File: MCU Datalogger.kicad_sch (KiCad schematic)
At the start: 0 parts

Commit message: configure schematic
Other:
- title: (none) -> ${project_name}
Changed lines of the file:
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@@
 	(generator_version "8.0")
 	(paper "A4")
+	(title_block
+		(title "${project_name}")
+		(date "2024-09-19")
+		(rev "1")
+	)
 	(sheet_instances
 		(path "/"

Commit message: arrange schematic symbols
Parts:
- added BT1: Battery, symbol Device:Battery
- added C1, C2, C3, C4: C, symbol Device:C
- added C5: C_Polarized, symbol Device:C_Polarized
- added D1, D2: LED, symbol Device:LED
- added H1, H2, H3, H4: MountingHole, symbol Mechanical:MountingHole
- added R1, R2, R3, R4, R5, R6, R7: R, symbol Device:R
- added U1, U2: 24LC1025, symbol Memory_EEPROM:24LC1025
- added U3: DS1337S_T_R, DS1337S_T_R:SOIC127P600X175-8N, symbol DS1337S_T_R:DS1337S_T_R
- added U4: ATMEGA328P-AN, ATMEGA328P-AN:QFP80P900X900X120-32N, symbol ATMEGA328P-AN:ATMEGA328P-AN
- added Y1, Y2: Crystal, symbol Device:Crystal
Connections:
- new net: U4.21 (GND), U4.3 (GND), U4.5 (GND)
- new net: U4.4 (VCC), U4.6 (VCC)
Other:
- added sheet Connectors (conenctors.kicad_sch)

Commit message: assign footprints
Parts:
- BT1: footprint (none) -> Connector_PinHeader_2.54mm:PinHeader_1x02_P2.54mm_Vertical
- C1, C2: value C -> 22pF; footprint (none) -> Capacitor_SMD:C_0805_2012Metric
- C3, C4: value C -> 0.1uF; footprint (none) -> Capacitor_SMD:C_0805_2012Metric
- C5: value C_Polarized -> 100nF; footprint (none) -> Capacitor_SMD:C_0805_2012Metric
- D1, D2: footprint (none) -> LED_SMD:LED_0805_2012Metric
- H1, H2, H3, H4: footprint (none) -> MountingHole:MountingHole_2.1mm
- R1, R2: value R -> 4.7K; footprint (none) -> Resistor_SMD:R_0805_2012Metric
- R3, R5: value R -> 330; footprint (none) -> Resistor_SMD:R_0805_2012Metric
- R4, R6, R7: value R -> 10K; footprint (none) -> Resistor_SMD:R_0805_2012Metric
- U1, U2: footprint (none) -> Package_SO:SOIC-8_5.23x5.23mm_P1.27mm
- Y1: value Crystal -> 32.768 KHz; footprint (none) -> Crystal:Crystal_SMD_5032-2Pin_5.0x3.2mm_HandSoldering
- Y2: value Crystal -> 16 MHz; footprint (none) -> Crystal:Crystal_SMD_5032-2Pin_5.0x3.2mm_HandSoldering
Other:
- moved on the sheet: C3, C5, R7, Y1

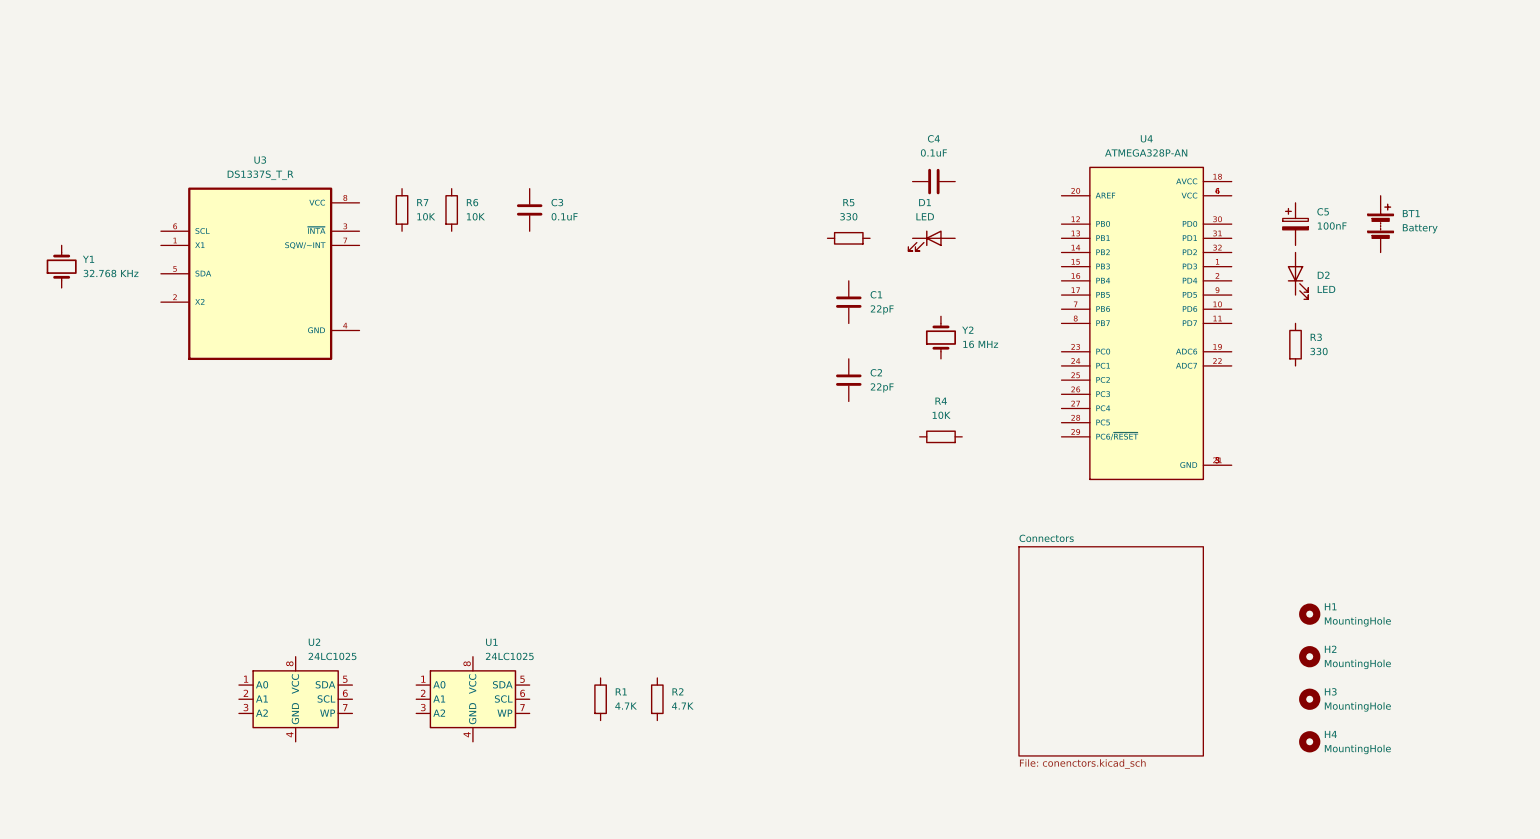
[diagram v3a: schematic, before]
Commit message: wire main scheme sheet
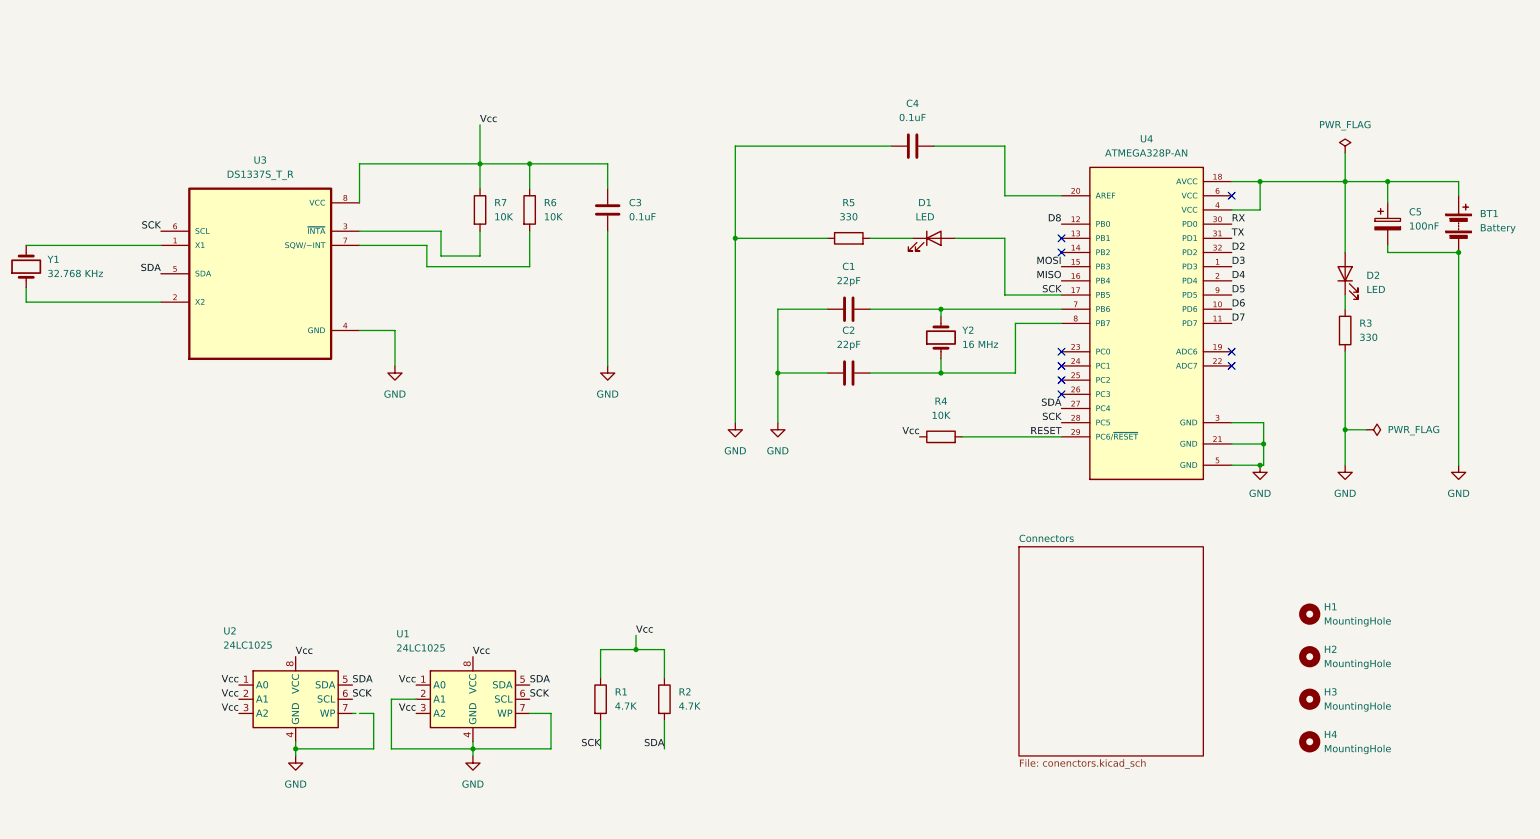
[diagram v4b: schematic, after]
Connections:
- net at Y1.1: now also U3.2 (X2)
- net at Y1.2: now also U3.1 (X1)
- net GND: now reaches C1.1
- net GND: now also BT1.2 (-), C2.1, C3.2, C4.1, C5.2, R3.2, R5.1, U1.2 (A1), U1.4 (GND), U1.7 (WP), U2.4 (GND), U3.4 (GND), U4.21 (GND), U4.3 (GND), U4.5 (GND)
- net at C1.2: now also U4.7 (PB6), Y2.2
- net Vcc: now reaches R4.1
- net Vcc: now also C3.1, R1.1, R2.1, R6.1, R7.1, U1.1 (A0), U1.3 (A2), U1.8 (VCC), U2.1 (A0), U2.2 (A1), U2.3 (A2), U2.8 (VCC), U3.8 (VCC)
- net RESET: now reaches R4.2
- net RESET: now also U4.29 (PC6/~{RESET})
- net at R6.2: now also U3.7 (SQW/~INT)
- net at R3.1: now also D2.1 (K)
- net at U3.3 (~{INTA}): now also R7.2
- net SDA: now reaches U3.5 (SDA)
- net SDA: now also R2.2, U1.5 (SDA), U2.5 (SDA), U4.27 (PC4)
- net SCK: now reaches U3.6 (SCL)
- net SCK: now also D1.2 (A), R1.2, U1.6 (SCL), U2.6 (SCL), U4.17 (PB5), U4.28 (PC5)
- net at BT1.1 (+): now also C5.1, D2.2 (A), U4.18 (AVCC), U4.4 (VCC)
- net at Y2.1: now also C2.2, U4.8 (PB7)
- net at D1.1 (K): now also R5.2
- net at C4.2: now also U4.20 (AREF)
- net D3: now reaches U4.1 (PD3)
- net D6: now reaches U4.10 (PD6)
- net D7: now reaches U4.11 (PD7)
- net D8: now reaches U4.12 (PB0)
- net MOSI: now reaches U4.15 (PB3)
- net MISO: now reaches U4.16 (PB4)
- net D4: now reaches U4.2 (PD4)
- net RX: now reaches U4.30 (PD0)
- net TX: now reaches U4.31 (PD1)
- net D2: now reaches U4.32 (PD2)
- net at U4.6 (VCC): no longer U4.4 (VCC)
- net D5: now reaches U4.9 (PD5)
- no-connect marks 0 -> 9
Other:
- moved on the sheet: BT1, C1, C2, C3, C4, C5, D2, R2, R3, R6, R7, Y1

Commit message: complete wiring and perform ERC
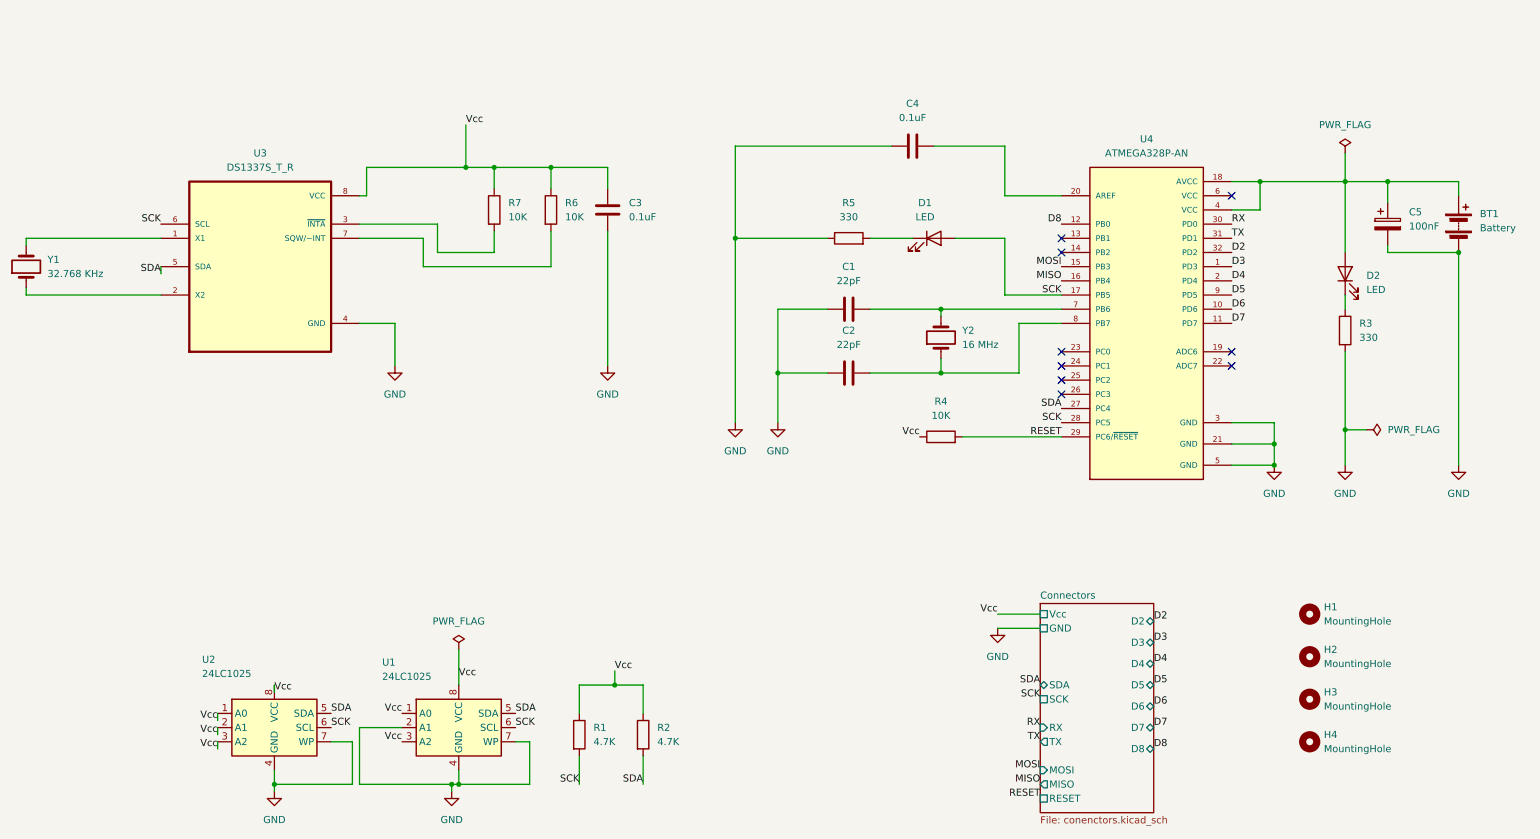
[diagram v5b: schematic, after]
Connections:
- net GND: now also U2.7 (WP)
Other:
- sheet Connectors ports: added D2, D3, D4, D5, D6, D7, D8, GND, MISO, MOSI, RESET, RX, SCK, SDA, TX, Vcc; removed none
- moved on the sheet: R1, R2, R6, R7, U1, U2, U3

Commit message: fix bugs
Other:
- note added: "EEPROM"
- note added: "MCU"
- note added: "Mounting"
- note added: "Real Time Clock"
- moved on the sheet: BT1, C1, C2, C3, C4, C5, D1, D2, H1, H2, H3, H4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
